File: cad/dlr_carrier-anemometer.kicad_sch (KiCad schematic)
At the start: 8 parts, among them J13 ANEMO_M12_5P, U7 SP3485EN

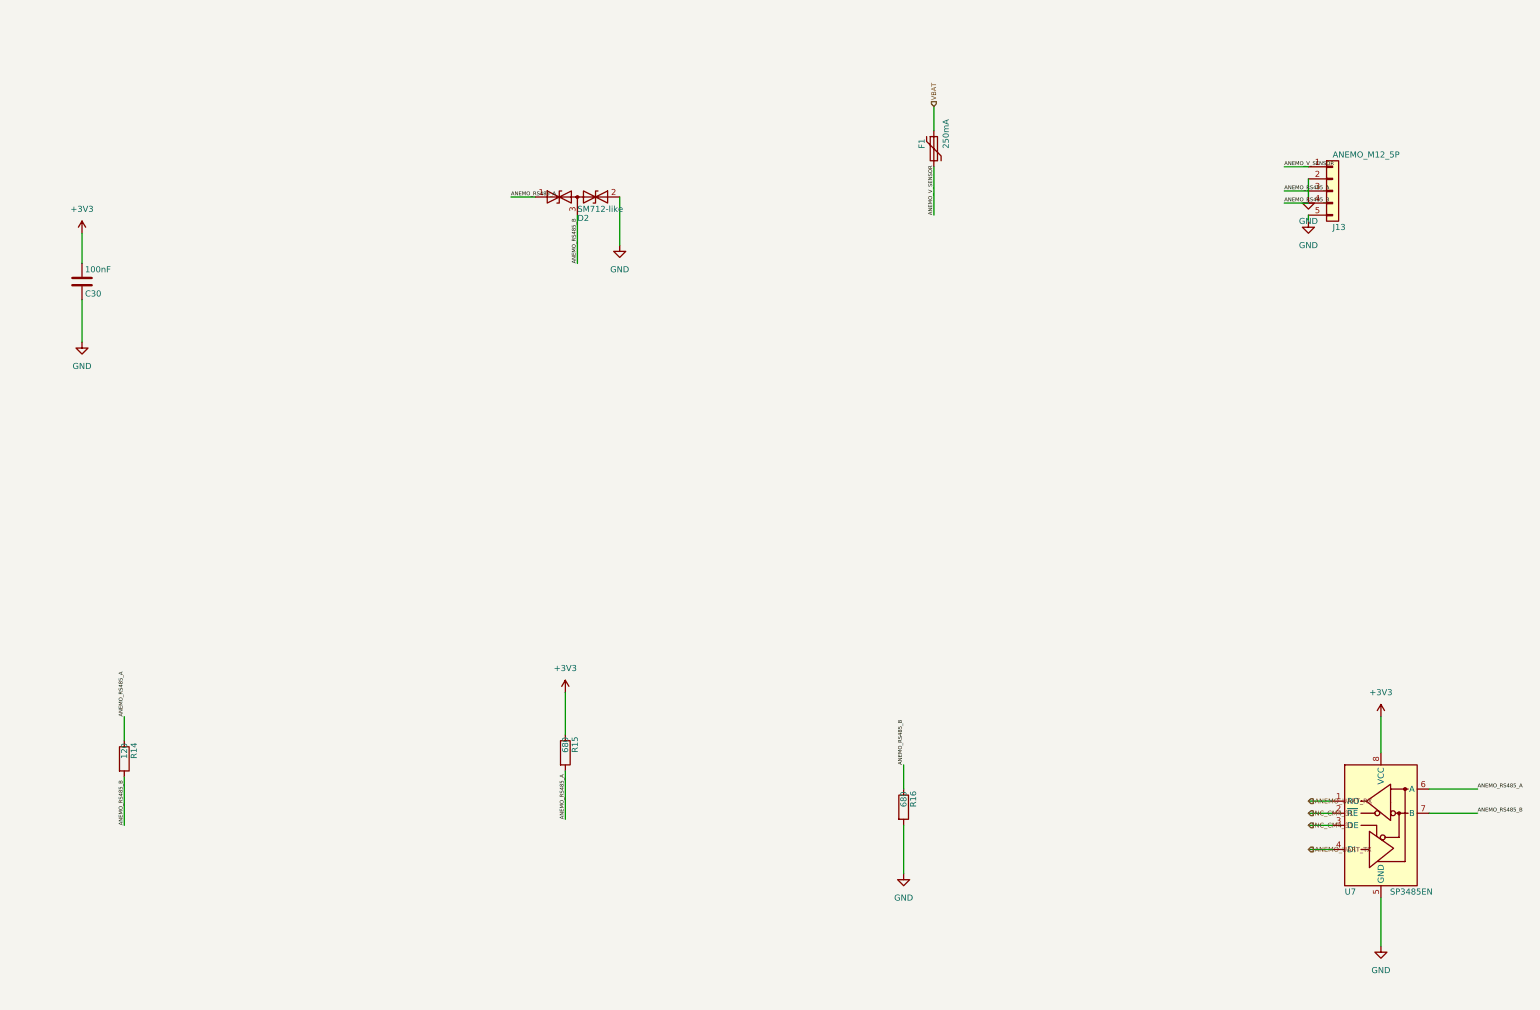
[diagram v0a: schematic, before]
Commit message: 🎨 style: lint fixes (f-string, unused imports, complexity, naming)
CI lint surface from the prior commit:
* F541: drop extraneous `f` prefixes on f-strings without placeholders
* F401: remove unused `math` and `_place_pwr_flags` imports
* C901: extract `_route_sheet_nets` helper so `build_child_sheet`
  complexity drops back under the McCabe threshold
* N806: lowercase local constants in `build_root_sheet`
* black: reformat multi_sheet.py + schematic.py

Co-Authored-By: Claude Opus 4.7 (1M context) <noreply@anthropic.com>
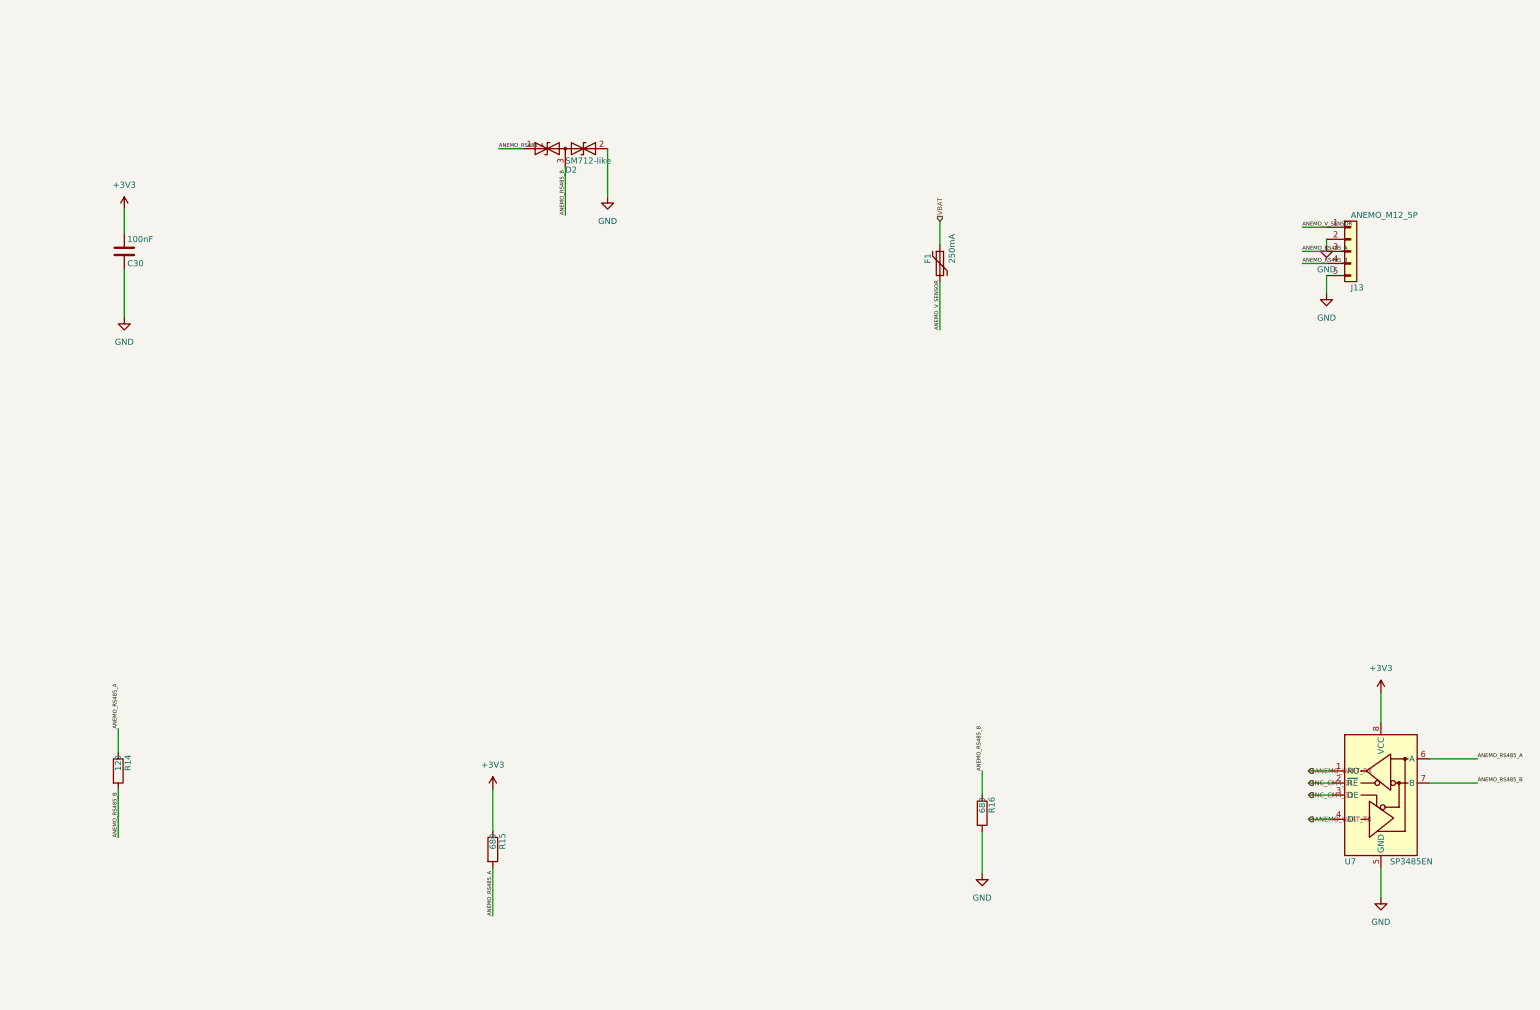
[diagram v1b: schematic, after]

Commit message: 🪪 feat(anemometer): low-wind variant — Vaisala WMT702, kit SKU split
Locks the low-wind variant per the grill-me design tree. Single PCB +
single firmware binary; the variant lives in the kit BOM (sensor + cable
harness + PV panel + battery). Both sensors speak NMEA 0183 over the
RS-485 transceiver so the driver is talker-agnostic.

Hardware:
* anemometer.py: add SMBJ24CA TVS on V+→GND for IEC 61000-4-5 2 kV
  surge tolerance (utility-tower deployment).

Theory:
* theory.ipynb §6: variant-aware power-budget cell. WMT702's 480 mW
  draw needs a 30 W panel + 100 Wh battery to hold 1.66× winter margin
  and 2.22 d autonomy. High-wind kit (Calypso, 1 mW) stays on the
  existing 20 W / 50 Wh baseline.
* Expected-values table rebuilt with per-variant rows.

README:
* New "Anemometer Variants" section: full kit BOM table, deployment
  decision rule (NREL WIND Toolkit climatology, 15 % yr V_w<1 m/s
  threshold), fallback policy, per-variant power numbers.

Co-Authored-By: Claude Opus 4.7 (1M context) <noreply@anthropic.com>
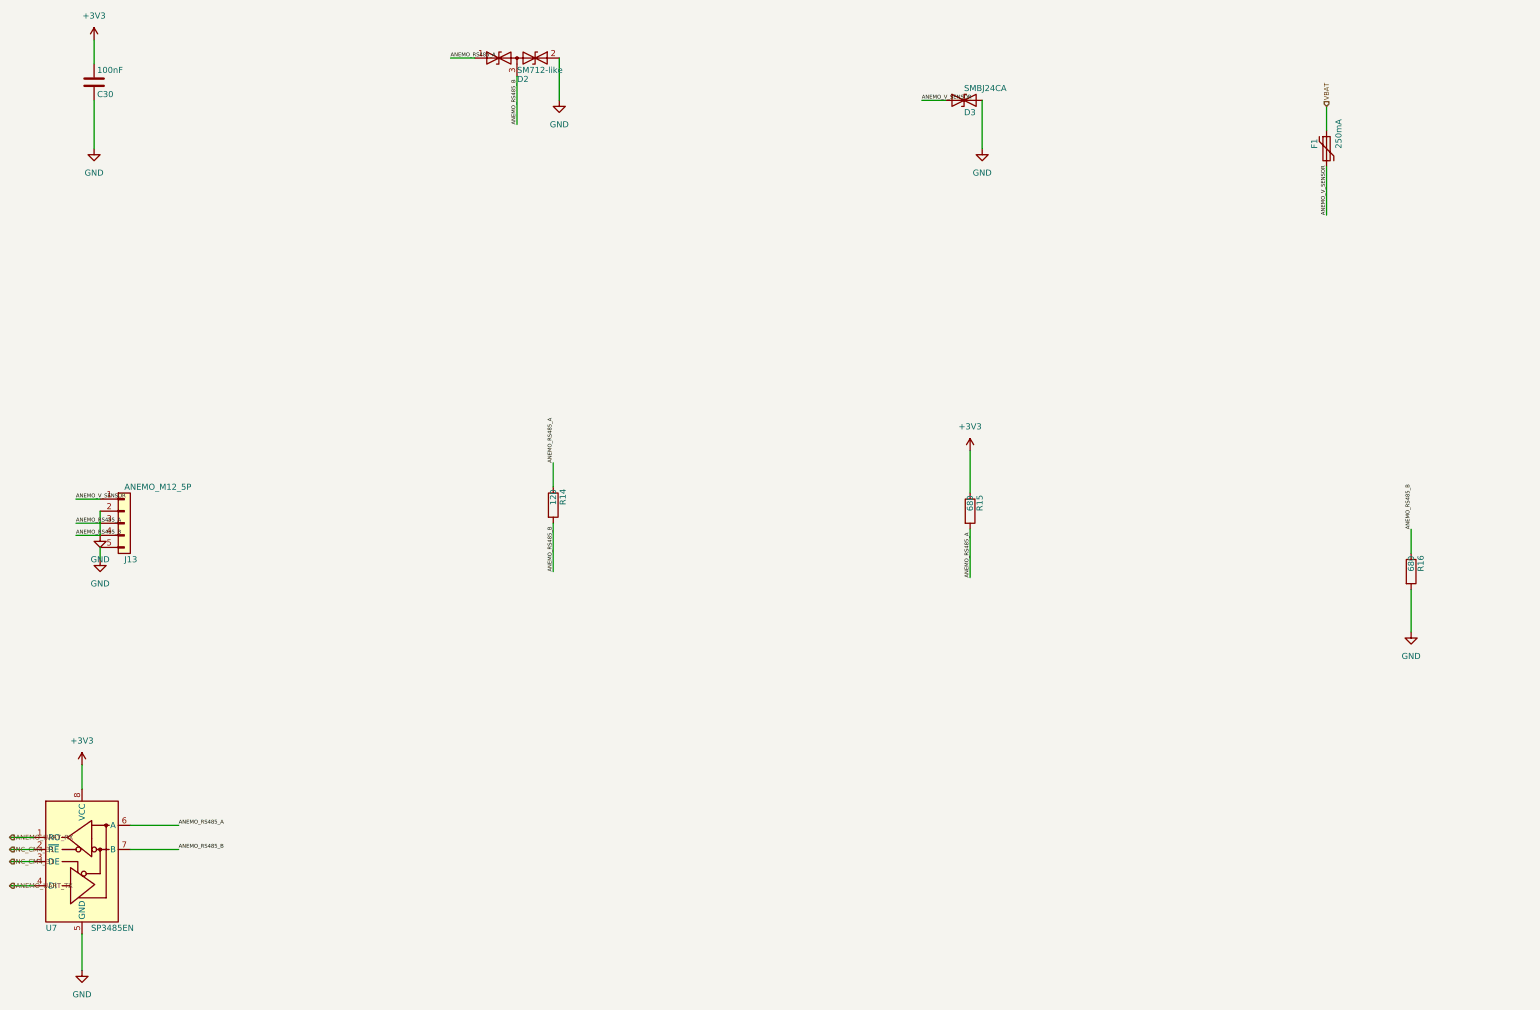
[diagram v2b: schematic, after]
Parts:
- added D3: SMBJ24CA, Package_TO_SOT_SMD:SOT-23, symbol Device:D_TVS
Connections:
- net ANEMO_RS485_B is gone; now on net GND: D2.3 (common), J13.4 (Pin_4), R14.2, R16.1, U7.7 (B)
- net ANEMO_V_SENSOR: now also D3.1 (A1)
- net GND: now also D3.2 (A2)
